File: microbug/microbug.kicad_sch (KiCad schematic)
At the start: 24 parts, among them J1 Conn_01x03, J2 Conn_01x03, J3 Conn_01x02, M1 Motor_DC, M2 Motor_DC, U1 ATtiny1616-S, U2 QRE1113GR, U3 TC78H651AFNG, U4 QRE1113GR

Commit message: switched driver ic for 660
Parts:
- removed U3: TC78H651AFNG, Package_SO:TSSOP-16_4.4x5mm_P0.65mm, symbol microbug-lib:TC78H651AFNG
- added R10: 10k, Resistor_SMD:R_0603_1608Metric_Pad1.05x0.95mm_HandSolder, symbol Device:R
- added R9: 47k, Resistor_SMD:R_0603_1608Metric_Pad1.05x0.95mm_HandSolder, symbol Device:R
- added U5: TC78H651AFNG, Package_SO:TSSOP-16_4.4x5mm_P0.65mm, symbol microbug-lib:TC78H651AFNG
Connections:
- net +3V3: now also R10.1, U5.12 (VREF), U5.5 (VM)
- net DIR1: now also U5.1 (En_A)
- net DIR2: now also U5.2 (En_B)
- net GND: now also R9.1, U5.11 (PGND_B), U5.4 (AGND), U5.6 (PGND_A)
- net PWM1: now also U1.13 (PC1), U5.3 (Phase_A); no longer U1.12 (PC0)
- net PWM2: now also U1.12 (PC0), U5.16 (Phase_B); no longer U1.13 (PC1)
- net at M1.1 (+): now also U5.7 (OUTA+)
- net at M1.2 (-): now also U5.8 (OUTA-)
- net at M2.1 (+): now also U5.10 (OUTB+)
- net at M2.2 (-): now also U5.9 (OUTB-)
- new net: R10.2, U5.14 (STBY)
- new net: R9.2, U5.13 (OSCM)
- no-connect marks 3 -> 4
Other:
- moved on the sheet: C2, C3, M1

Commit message: added note
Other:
- note added: "I assume these were connected differently in the PCB for a reason? (specifically r2 and r4)"
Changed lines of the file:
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@@
     (effects (font (size 2.54 2.54)) (justify left bottom))
+  )
+  (text "I assume these were connected differently in the PCB for a reason?\n(specifically r2 and r4)\n"
+    (at 190.627 152.781 0)
+    (effects (font (size 1.27 1.27)) (justify left bottom))
   )
   (text "Motors" (at 191.77 46.99 0)

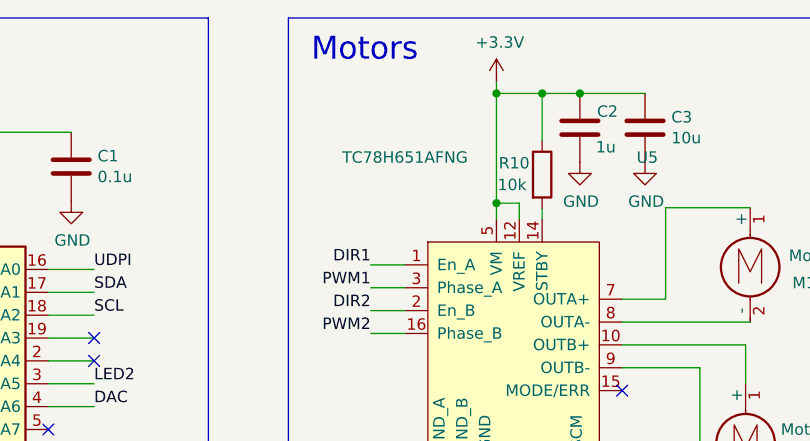
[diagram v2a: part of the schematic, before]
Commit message: fixed driver ic symbol name
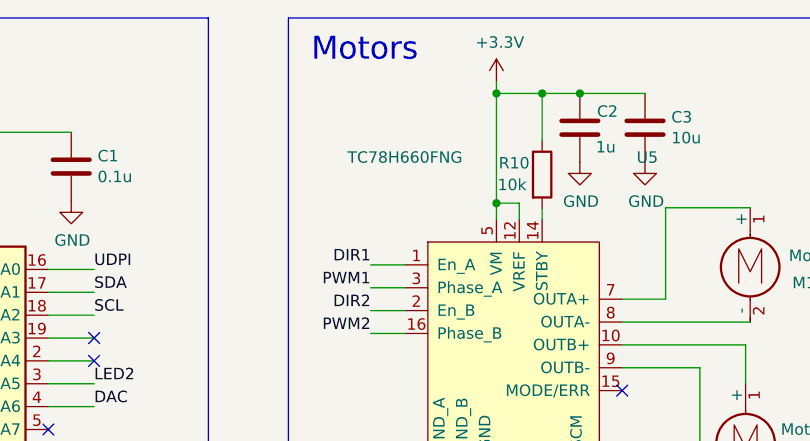
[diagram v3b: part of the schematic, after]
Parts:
- U5: value TC78H651AFNG -> TC78H660FNG
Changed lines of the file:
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@@
     (in_bom yes) (on_board yes)
     (property "Reference" "U5" (id 0) (at 229.108 57.404 0))
-    (property "Value" "TC78H651AFNG" (id 1) (at 202.184 57.404 0))
+    (property "Value" "TC78H660FNG" (id 1) (at 202.184 57.404 0))
     (property "Footprint" "Package_SO:TSSOP-16_4.4x5mm_P0.65mm" (id 2) (at 212.344 85.852 0)
       (effects (font (size 1.27 1.27)) hide)
@@
     )
     (path "/3014f0b8-0092-432c-bc72-38f86faad22e"
-      (reference "U5") (unit 1) (value "TC78H651AFNG") (footprint "Package_SO:TSSOP-16_4.4x5mm_P0.65mm")
-    )
-  )
+      (reference "U5") (unit 1) (value "TC78H660FNG") (footprint "Package_SO:TSSOP-16_4.4x5mm_P0.65mm")
+    )
+  )

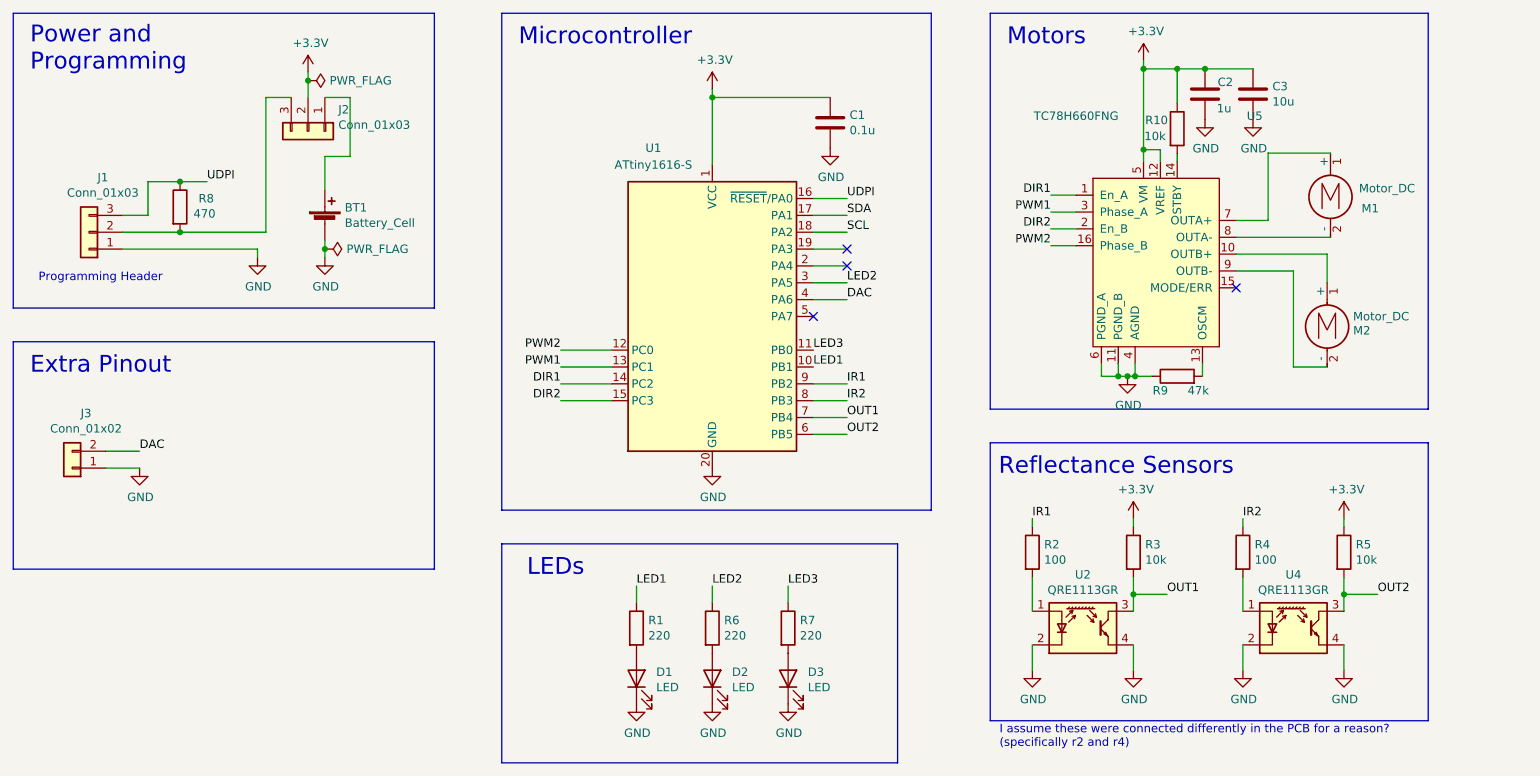
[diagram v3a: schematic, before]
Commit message: fixed programming header stuff and qre111 symbol stuff
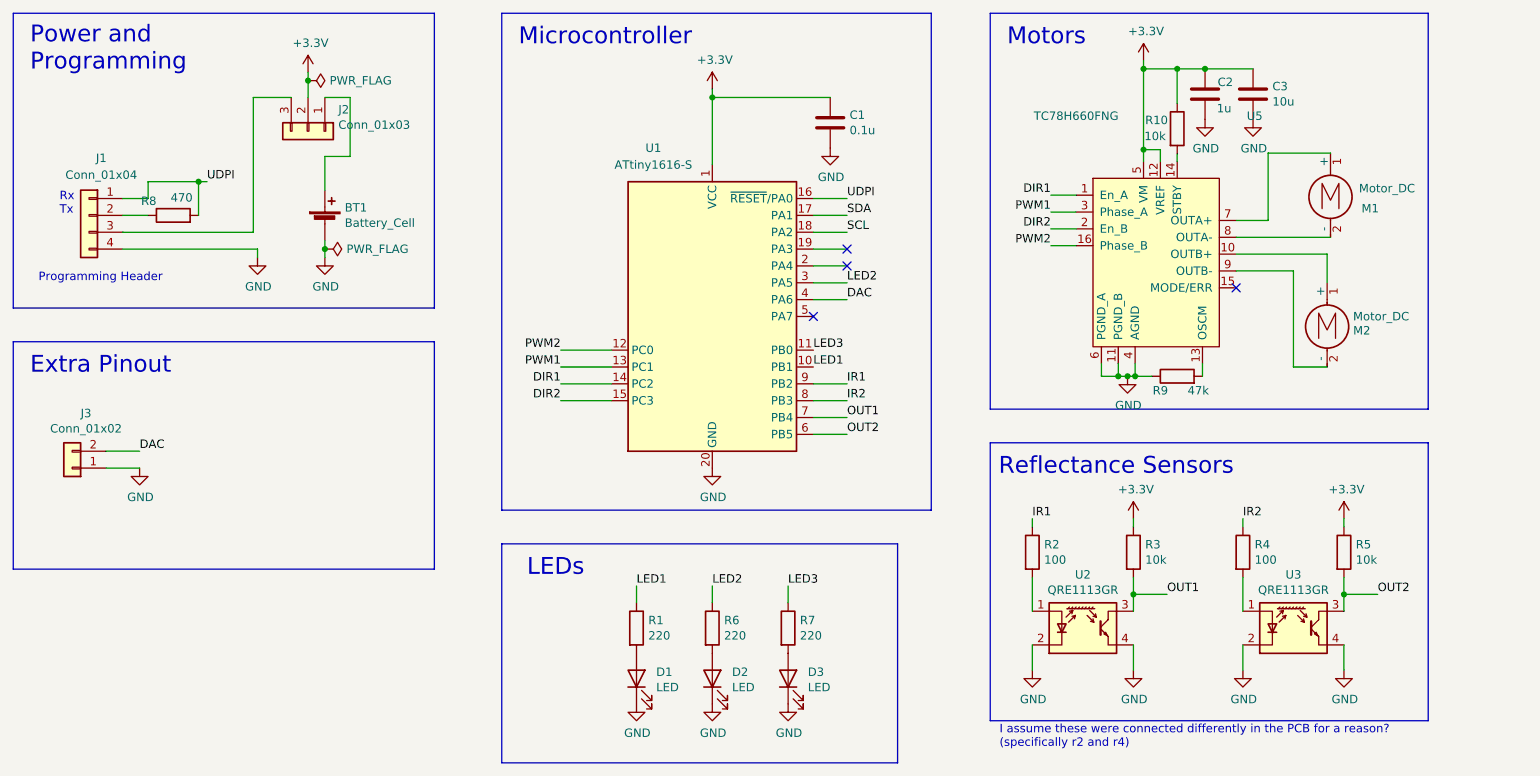
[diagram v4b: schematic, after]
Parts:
- removed J1: Conn_01x03, Connector_PinHeader_2.54mm:PinHeader_1x03_P2.54mm_Vertical, symbol Connector_Generic:Conn_01x03
- removed U4: QRE1113GR, OptoDevice:Everlight_ITR8307F43, symbol Sensor_Proximity:QRE1113GR
- added J1: Conn_01x04, Connector_PinHeader_2.54mm:PinHeader_1x04_P2.54mm_Vertical, symbol Connector_Generic:Conn_01x04
- added U3: QRE1113GR, OptoDevice:OnSemi_CASE100CY, symbol Sensor_Proximity:QRE1113GR
- U2: footprint OptoDevice:Everlight_ITR8307F43 -> OptoDevice:OnSemi_CASE100CY
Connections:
- net GND: now also J1.4 (Pin_4), U3.2 (K), U3.4
- net OUT2: now also U3.3
- net UDPI: now also R8.2, J1.1 (Pin_1); no longer R8.1
- net at J2.3 (Pin_3): now also J1.3 (Pin_3); no longer R8.2
- net at R4.2: now also U3.1 (A)
- new net: J1.2 (Pin_2), R8.1
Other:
- note added: "Rx Tx"
- moved on the sheet: R8
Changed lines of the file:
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@@
 (kicad_sch (version 20210621) (generator eeschema)
   (paper "A4")
-  (junction (at 67.056 67.31) (diameter 0) (color 0 0 0 0))
-  (junction (at 67.056 74.93) (diameter 0) (color 0 0 0 0))
+  (junction (at 69.85 67.31) (diameter 0) (color 0 0 0 0))
   (junction (at 86.36 52.07) (diameter 0) (color 0 0 0 0))
   (junction (at 88.9 77.47) (diameter 0) (color 0 0 0 0))
@@
     (stroke (width 0) (type default) (color 0 0 0 0))
   )
-  (wire (pts (xy 58.42 74.93) (xy 67.056 74.93))
+  (wire (pts (xy 58.42 74.93) (xy 78.105 74.93))
     (stroke (width 0) (type default) (color 0 0 0 0))
   )
@@
     (stroke (width 0) (type default) (color 0 0 0 0))
   )
-  (wire (pts (xy 62.23 67.31) (xy 62.23 72.39))
-    (stroke (width 0) (type default) (color 0 0 0 0))
-  )
-  (wire (pts (xy 62.23 67.31) (xy 67.056 67.31))
+  (wire (pts (xy 62.23 67.31) (xy 62.23 69.85))
+    (stroke (width 0) (type default) (color 0 0 0 0))
+  )
+  (wire (pts (xy 62.23 67.31) (xy 69.85 67.31))
+    (stroke (width 0) (type default) (color 0 0 0 0))
+  )
+  (wire (pts (xy 62.23 69.85) (xy 58.42 69.85))
     (stroke (width 0) (type default) (color 0 0 0 0))
   )
@@
     (stroke (width 0) (type default) (color 0 0 0 0))
   )
-  (wire (pts (xy 67.056 67.31) (xy 71.12 67.31))
-    (stroke (width 0) (type default) (color 0 0 0 0))
-  )
-  (wire (pts (xy 67.056 74.93) (xy 80.01 74.93))
+  (wire (pts (xy 69.85 67.31) (xy 71.12 67.31))
+    (stroke (width 0) (type default) (color 0 0 0 0))
+  )
+  (wire (pts (xy 69.85 72.39) (xy 69.85 67.31))
+    (stroke (width 0) (type default) (color 0 0 0 0))
+  )
+  (wire (pts (xy 78.105 54.61) (xy 78.105 74.93))
+    (stroke (width 0) (type default) (color 0 0 0 0))
+  )
+  (wire (pts (xy 78.105 54.61) (xy 83.82 54.61))
     (stroke (width 0) (type default) (color 0 0 0 0))
   )
   (wire (pts (xy 78.74 77.47) (xy 78.74 78.74))
-    (stroke (width 0) (type default) (color 0 0 0 0))
-  )
-  (wire (pts (xy 80.01 54.61) (xy 80.01 74.93))
-    (stroke (width 0) (type default) (color 0 0 0 0))
-  )
-  (wire (pts (xy 83.82 54.61) (xy 80.01 54.61))
     (stroke (width 0) (type default) (color 0 0 0 0))
   )
@@
     (effects (font (size 1.27 1.27)) (justify left bottom))
   )
+  (text "Rx\nTx\n" (at 48.895 72.39 0)
+    (effects (font (size 1.27 1.27)) (justify left bottom))
+  )
   (text "Microcontroller" (at 118.11 46.99 0)
     (effects (font (size 2.54 2.54)) (justify left bottom))
@@
     (pin "1")
   )
-  (symbol (lib_id "Device:R") (at 67.056 71.12 0) (unit 1)
-    (in_bom yes) (on_board yes)
-    (property "Reference" "R8" (id 0) (at 69.85 69.8499 0)
-      (effects (font (size 1.27 1.27)) (justify left))
-    )
-    (property "Value" "470" (id 1) (at 69.088 72.1359 0)
-      (effects (font (size 1.27 1.27)) (justify left))
-    )
-    (property "Footprint" "Resistor_SMD:R_0603_1608Metric_Pad1.05x0.95mm_HandSolder" (id 2) (at 65.278 71.12 90)
-      (effects (font (size 1.27 1.27)) hide)
-    )
-    (property "Datasheet" "~" (id 3) (at 67.056 71.12 0)
+  (symbol (lib_id "Device:R") (at 66.04 72.39 90) (unit 1)
+    (in_bom yes) (on_board yes)
+    (property "Reference" "R8" (id 0) (at 63.4999 70.231 90)
+      (effects (font (size 1.27 1.27)) (justify left))
+    )
+    (property "Value" "470" (id 1) (at 68.9609 69.723 90)
+      (effects (font (size 1.27 1.27)) (justify left))
+    )
+    (property "Footprint" "Resistor_SMD:R_0603_1608Metric_Pad1.05x0.95mm_HandSolder" (id 2) (at 66.04 74.168 90)
+      (effects (font (size 1.27 1.27)) hide)
+    )
+    (property "Datasheet" "~" (id 3) (at 66.04 72.39 0)
       (effects (font (size 1.27 1.27)) hide)
     )
@@
     (pin "2")
   )
-  (symbol (lib_id "Connector_Generic:Conn_01x03") (at 53.34 74.93 180) (unit 1)
-    (in_bom yes) (on_board yes)
-    (property "Reference" "J1" (id 0) (at 55.4228 66.675 0))
-    (property "Value" "Conn_01x03" (id 1) (at 55.4228 68.9864 0))
-    (property "Footprint" "Connector_PinHeader_2.54mm:PinHeader_1x03_P2.54mm_Vertical" (id 2) (at 53.34 74.93 0)
-      (effects (font (size 1.27 1.27)) hide)
-    )
-    (property "Datasheet" "~" (id 3) (at 53.34 74.93 0)
+  (symbol (lib_id "Connector_Generic:Conn_01x03") (at 86.36 59.69 270) (unit 1)
+    (in_bom yes) (on_board yes)
+    (property "Reference" "J2" (id 0) (at 90.932 56.4388 90)
+      (effects (font (size 1.27 1.27)) (justify left))
+    )
+    (property "Value" "Conn_01x03" (id 1) (at 90.932 58.7502 90)
+      (effects (font (size 1.27 1.27)) (justify left))
+    )
+    (property "Footprint" "Connector_PinHeader_2.54mm:PinHeader_1x03_P2.54mm_Vertical" (id 2) (at 86.36 59.69 0)
+      (effects (font (size 1.27 1.27)) hide)
+    )
+    (property "Datasheet" "~" (id 3) (at 86.36 59.69 0)
       (effects (font (size 1.27 1.27)) hide)
     )
@@
     (pin "3")
   )
-  (symbol (lib_id "Connector_Generic:Conn_01x03") (at 86.36 59.69 270) (unit 1)
-    (in_bom yes) (on_board yes)
-    (property "Reference" "J2" (id 0) (at 90.932 56.4388 90)
-      (effects (font (size 1.27 1.27)) (justify left))
-    )
-    (property "Value" "Conn_01x03" (id 1) (at 90.932 58.7502 90)
-      (effects (font (size 1.27 1.27)) (justify left))
-    )
-    (property "Footprint" "Connector_PinHeader_2.54mm:PinHeader_1x03_P2.54mm_Vertical" (id 2) (at 86.36 59.69 0)
-      (effects (font (size 1.27 1.27)) hide)
-    )
-    (property "Datasheet" "~" (id 3) (at 86.36 59.69 0)
+  (symbol (lib_id "Connector_Generic:Conn_01x04") (at 53.34 72.39 0) (mirror y) (unit 1)
+    (in_bom yes) (on_board yes)
+    (property "Reference" "J1" (id 0) (at 55.1815 63.754 0))
+    (property "Value" "Conn_01x04" (id 1) (at 55.1815 66.294 0))
+    (property "Footprint" "Connector_PinHeader_2.54mm:PinHeader_1x04_P2.54mm_Vertical" (id 2) (at 53.34 72.39 0)
+      (effects (font (size 1.27 1.27)) hide)
+    )
+    (property "Datasheet" "~" (id 3) (at 53.34 72.39 0)
       (effects (font (size 1.27 1.27)) hide)
     )
@@
     (pin "2")
     (pin "3")
+    (pin "4")
   )
   (symbol (lib_id "Motor:Motor_DC") (at 240.03 87.63 0) (mirror y) (unit 1)
@@
     (property "Reference" "U2" (id 0) (at 203.2 126.5682 0))
     (property "Value" "QRE1113GR" (id 1) (at 203.2 128.8796 0))
-    (property "Footprint" "OptoDevice:Everlight_ITR8307F43" (id 2) (at 203.2 139.7 0)
+    (property "Footprint" "OptoDevice:OnSemi_CASE100CY" (id 2) (at 203.2 139.7 0)
       (effects (font (size 1.27 1.27)) hide)
     )
@@
   (symbol (lib_id "Sensor_Proximity:QRE1113GR") (at 234.95 134.62 0) (unit 1)
     (in_bom yes) (on_board yes)
-    (property "Reference" "U4" (id 0) (at 234.95 126.5682 0))
+    (property "Reference" "U3" (id 0) (at 234.95 126.5682 0))
     (property "Value" "QRE1113GR" (id 1) (at 234.95 128.8796 0))
-    (property "Footprint" "OptoDevice:Everlight_ITR8307F43" (id 2) (at 234.95 139.7 0)
+    (property "Footprint" "OptoDevice:OnSemi_CASE100CY" (id 2) (at 234.95 139.7 0)
       (effects (font (size 1.27 1.27)) hide)
     )
@@
       (reference "D3") (unit 1) (value "LED") (footprint "LED_SMD:LED_0603_1608Metric_Pad1.05x0.95mm_HandSolder")
     )
-    (path "/00000000-0000-0000-0000-00005e545f87"
-      (reference "J1") (unit 1) (value "Conn_01x03") (footprint "Connector_PinHeader_2.54mm:PinHeader_1x03_P2.54mm_Vertical")
+    (path "/8951631c-7a8e-4f41-b6ed-40b357def0bf"
+      (reference "J1") (unit 1) (value "Conn_01x04") (footprint "Connector_PinHeader_2.54mm:PinHeader_1x04_P2.54mm_Vertical")
     )
     (path "/00000000-0000-0000-0000-00005e5d0ac8"
@@
     )
     (path "/00000000-0000-0000-0000-00005e57b1a8"
-      (reference "U2") (unit 1) (value "QRE1113GR") (footprint "OptoDevice:Everlight_ITR8307F43")
-    )
-    (path "/00000000-0000-0000-0000-00005e58c03c"
-      (reference "U4") (unit 1) (value "QRE1113GR") (footprint "OptoDevice:Everlight_ITR8307F43")
+      (reference "U2") (unit 1) (value "QRE1113GR") (footprint "OptoDevice:OnSemi_CASE100CY")
+    )
+    (path "/f53ef5ec-fda6-4258-abae-1af6eb4f346d"
+      (reference "U3") (unit 1) (value "QRE1113GR") (footprint "OptoDevice:OnSemi_CASE100CY")
     )
     (path "/3014f0b8-0092-432c-bc72-38f86faad22e"

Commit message: pulled up mode pin
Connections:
- net +3V3: now also U5.15 (MODE/ERR)
- no-connect marks 4 -> 3
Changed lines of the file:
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@@
   (junction (at 217.424 50.292) (diameter 0) (color 0 0 0 0))
   (junction (at 221.615 50.292) (diameter 0) (color 0 0 0 0))
+  (junction (at 226.441 50.292) (diameter 0) (color 0 0 0 0))
   (junction (at 242.57 129.54) (diameter 0) (color 0 0 0 0))
   (no_connect (at 162.56 87.63))
   (no_connect (at 167.64 77.47))
   (no_connect (at 167.64 80.01))
-  (no_connect (at 226.314 83.312))
   (wire (pts (xy 55.88 107.95) (xy 60.96 107.95))
     (stroke (width 0) (type default) (color 0 0 0 0))
@@
     (stroke (width 0) (type default) (color 0 0 0 0))
   )
-  (wire (pts (xy 221.615 50.292) (xy 228.854 50.292))
+  (wire (pts (xy 221.615 50.292) (xy 226.441 50.292))
     (stroke (width 0) (type default) (color 0 0 0 0))
   )
@@
     (stroke (width 0) (type default) (color 0 0 0 0))
   )
+  (wire (pts (xy 226.314 83.312) (xy 226.441 83.312))
+    (stroke (width 0) (type default) (color 0 0 0 0))
+  )
+  (wire (pts (xy 226.441 50.292) (xy 228.854 50.292))
+    (stroke (width 0) (type default) (color 0 0 0 0))
+  )
+  (wire (pts (xy 226.441 83.312) (xy 226.441 50.292))
+    (stroke (width 0) (type default) (color 0 0 0 0))
+  )
